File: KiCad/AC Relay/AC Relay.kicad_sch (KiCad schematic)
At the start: 17 parts, among them J1 Screw_Terminal_01x02, J2 Conn_01x06_Female, J3 Screw_Terminal_01x02, K1 1-2071556-1, Q1 FDN537N, SW1 SW_Push, U1 BU33SD5WG-TR, U2 ESP-12E, U3 HLK-PM01

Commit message: initial commit
this is the intitial commit
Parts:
- U2: now not fitted

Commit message: title edited
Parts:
- U2: now fitted
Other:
- title: AC Relay -> BDBM

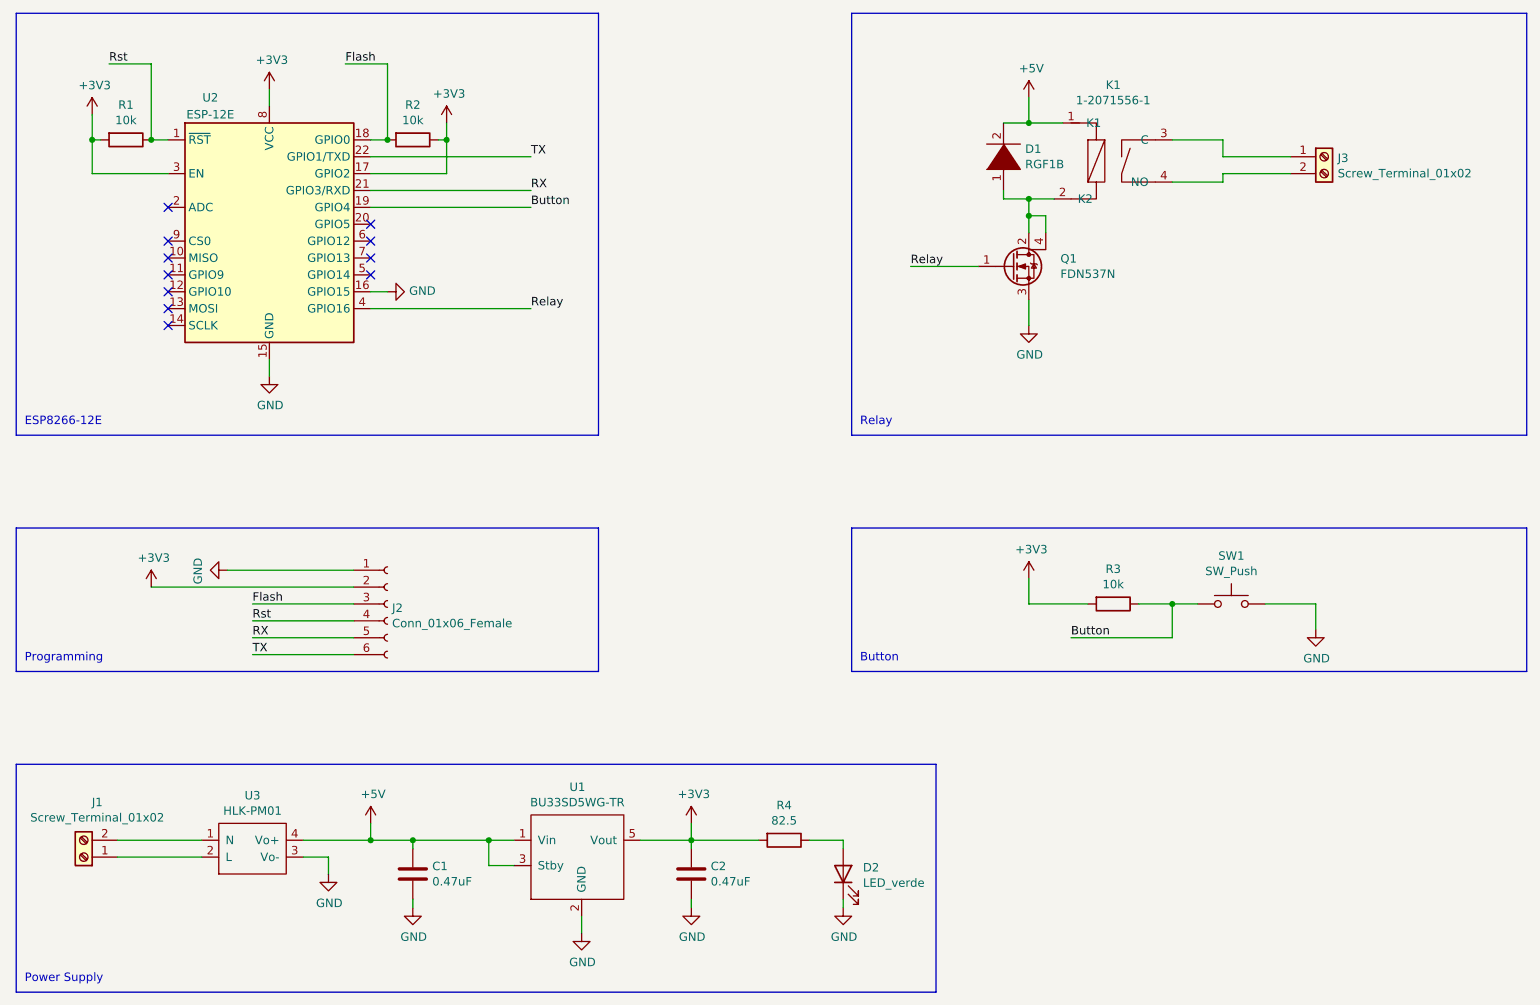
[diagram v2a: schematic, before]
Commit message: until components placemaent
done all until com placement, but had isssue in edge cut .
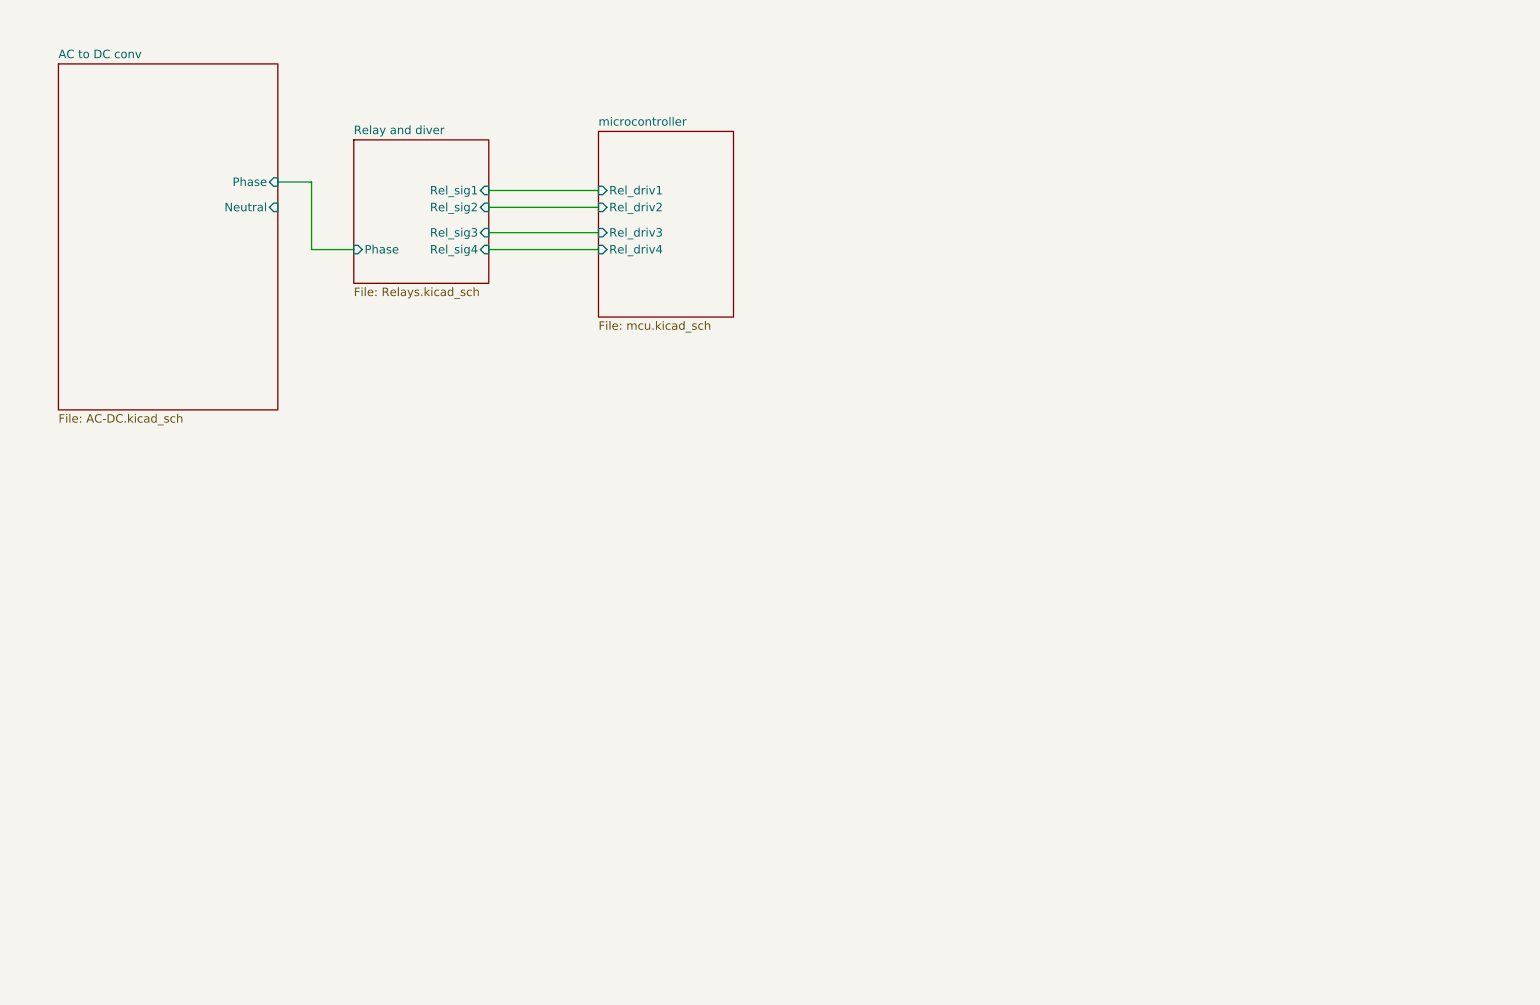
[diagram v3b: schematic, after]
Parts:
- removed C1, C2: 0.47uF, Capacitor_SMD:C_0603_1608Metric, symbol Device:C
- removed D1: RGF1B, Diode_SMD:D_0603_1608Metric, symbol pspice:DIODE
- removed D2: LED_verde, LED_SMD:LED_0603_1608Metric, symbol Device:LED
- removed J1, J3: Screw_Terminal_01x02, TerminalBlock:TerminalBlock_Altech_AK300-2_P5.00mm, symbol Connector:Screw_Terminal_01x02
- removed J2: Conn_01x06_Female, Connector_PinHeader_2.54mm:PinHeader_1x06_P2.54mm_Vertical, symbol Connector:Conn_01x06_Female
- removed K1: 1-2071556-1, red:Rele-1461492-2, symbol AC-Relay-rescue:Relay-red-MQTT-and-Google-Home-from-RED-rescue-AC-Relay-rescue-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
- removed Q1: FDN537N, Package_TO_SOT_SMD:SOT-223, symbol Device:Q_NMOS_GDSD
- removed R1, R2, R3: 10k, Resistor_SMD:R_0603_1608Metric_Pad1.05x0.95mm_HandSolder, symbol Device:R
- removed R4: 82.5, Resistor_SMD:R_0603_1608Metric_Pad1.05x0.95mm_HandSolder, symbol Device:R
- removed SW1: SW_Push, Button_Switch_SMD:SW_SPST_EVQP2, symbol Switch:SW_Push
- removed U1: BU33SD5WG-TR, Package_SO:TSOP-5_1.65x3.05mm_P0.95mm, symbol red:BU33SD5WG-TR
- removed U2: ESP-12E, RF_Module:ESP-12E, symbol RF_Module:ESP-12E
- removed U3: HLK-PM01, red:HLK-PM01, symbol red:HLK-PM01
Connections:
- no-connect marks 11 -> 0
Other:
- added sheet AC to DC conv (AC-DC.kicad_sch)
- added sheet Relay and diver (Relays.kicad_sch)
- added sheet microcontroller (mcu.kicad_sch)
- note removed: "Button"
- note removed: "ESP8266-12E"
- note removed: "Power Supply"
- note removed: "Programming"
- note removed: "Relay"

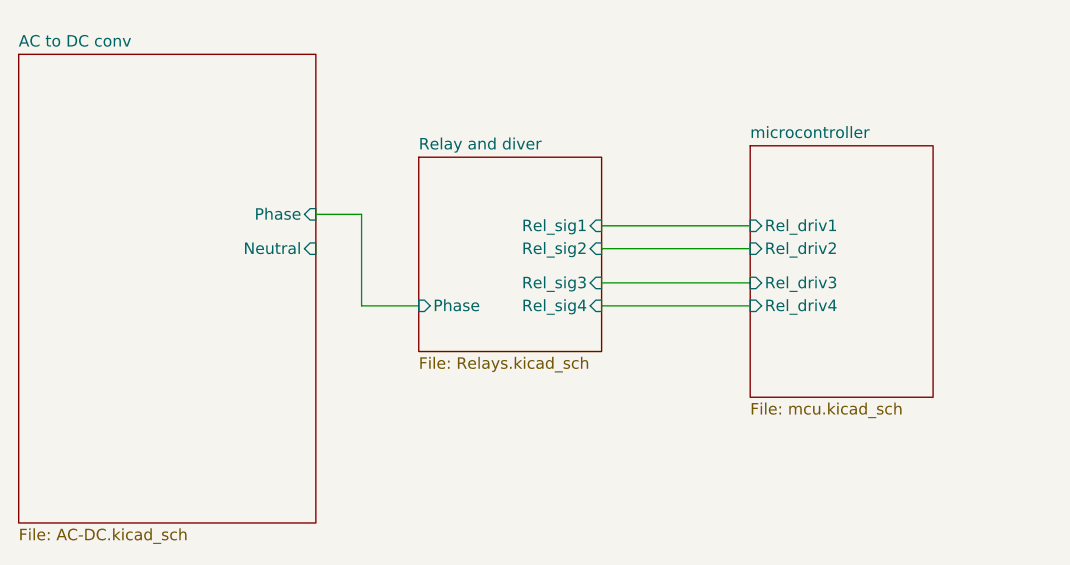
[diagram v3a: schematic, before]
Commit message: error elemination
schametic error elemination
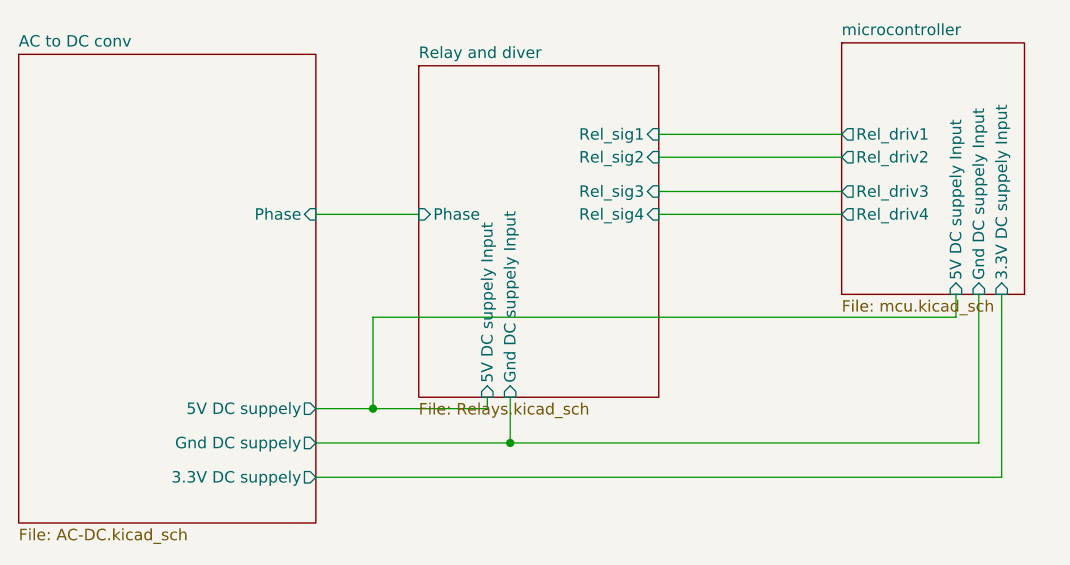
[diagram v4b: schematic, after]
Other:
- sheet AC to DC conv ports: added 3.3V DC suppely, 5V DC suppely, Gnd DC suppely; removed Neutral
- sheet Relay and diver ports: added 5V DC suppely Input, Gnd DC suppely Input; removed none
- sheet microcontroller ports: added 3.3V DC suppely Input, 5V DC suppely Input, Gnd DC suppely Input; removed none
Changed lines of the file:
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@@
 		(comment 1 "Designed by Raksh")
 	)
-	(wire
-		(pts
-			(xy 95.25 59.69) (xy 111.76 59.69)
-		)
-		(stroke
-			(width 0)
-			(type default)
-		)
-	)
-	(wire
-		(pts
-			(xy 68.58 55.88) (xy 63.5 55.88)
-		)
-		(stroke
-			(width 0)
-			(type default)
-		)
-	)
-	(wire
-		(pts
-			(xy 95.25 66.04) (xy 111.76 66.04)
-		)
-		(stroke
-			(width 0)
-			(type default)
-		)
-	)
-	(wire
-		(pts
-			(xy 95.25 57.15) (xy 111.76 57.15)
-		)
-		(stroke
-			(width 0)
-			(type default)
-		)
-	)
-	(wire
-		(pts
-			(xy 74.93 66.04) (xy 68.58 66.04)
-		)
-		(stroke
-			(width 0)
-			(type default)
-		)
-	)
-	(wire
-		(pts
-			(xy 68.58 66.04) (xy 68.58 55.88)
-		)
-		(stroke
-			(width 0)
-			(type default)
-		)
-	)
-	(wire
-		(pts
-			(xy 95.25 63.5) (xy 111.76 63.5)
+	(junction
+		(at 85.09 81.28)
+		(diameter 0)
+		(color 0 0 0 0)
+	)
+	(junction
+		(at 69.85 77.47)
+		(diameter 0)
+		(color 0 0 0 0)
+	)
+	(wire
+		(pts
+			(xy 85.09 81.28) (xy 85.09 76.2)
+		)
+		(stroke
+			(width 0)
+			(type default)
+		)
+	)
+	(wire
+		(pts
+			(xy 69.85 67.31) (xy 134.62 67.31)
+		)
+		(stroke
+			(width 0)
+			(type default)
+		)
+	)
+	(wire
+		(pts
+			(xy 63.5 81.28) (xy 85.09 81.28)
+		)
+		(stroke
+			(width 0)
+			(type default)
+		)
+	)
+	(wire
+		(pts
+			(xy 63.5 77.47) (xy 69.85 77.47)
+		)
+		(stroke
+			(width 0)
+			(type default)
+		)
+	)
+	(wire
+		(pts
+			(xy 63.5 55.88) (xy 74.93 55.88)
+		)
+		(stroke
+			(width 0)
+			(type default)
+		)
+	)
+	(wire
+		(pts
+			(xy 101.6 46.99) (xy 121.92 46.99)
+		)
+		(stroke
+			(width 0)
+			(type default)
+		)
+	)
+	(wire
+		(pts
+			(xy 121.92 53.34) (xy 101.6 53.34)
+		)
+		(stroke
+			(width 0)
+			(type default)
+		)
+	)
+	(wire
+		(pts
+			(xy 69.85 77.47) (xy 69.85 67.31)
+		)
+		(stroke
+			(width 0)
+			(type default)
+		)
+	)
+	(wire
+		(pts
+			(xy 134.62 67.31) (xy 134.62 64.77)
+		)
+		(stroke
+			(width 0)
+			(type default)
+		)
+	)
+	(wire
+		(pts
+			(xy 85.09 81.28) (xy 137.16 81.28)
+		)
+		(stroke
+			(width 0)
+			(type default)
+		)
+	)
+	(wire
+		(pts
+			(xy 139.7 64.77) (xy 139.7 85.09)
+		)
+		(stroke
+			(width 0)
+			(type default)
+		)
+	)
+	(wire
+		(pts
+			(xy 139.7 85.09) (xy 63.5 85.09)
+		)
+		(stroke
+			(width 0)
+			(type default)
+		)
+	)
+	(wire
+		(pts
+			(xy 101.6 49.53) (xy 121.92 49.53)
+		)
+		(stroke
+			(width 0)
+			(type default)
+		)
+	)
+	(wire
+		(pts
+			(xy 121.92 55.88) (xy 101.6 55.88)
+		)
+		(stroke
+			(width 0)
+			(type default)
+		)
+	)
+	(wire
+		(pts
+			(xy 82.55 77.47) (xy 82.55 76.2)
+		)
+		(stroke
+			(width 0)
+			(type default)
+		)
+	)
+	(wire
+		(pts
+			(xy 137.16 81.28) (xy 137.16 64.77)
+		)
+		(stroke
+			(width 0)
+			(type default)
+		)
+	)
+	(wire
+		(pts
+			(xy 69.85 77.47) (xy 82.55 77.47)
 		)
 		(stroke
@@
 			)
 		)
-		(pin "Neutral" input
-			(at 63.5 59.69 0)
+		(pin "3.3V DC suppely" output
+			(at 63.5 85.09 0)
+			(effects
+				(font
+					(size 1.27 1.27)
+				)
+				(justify right)
+			)
+		)
+		(pin "5V DC suppely" output
+			(at 63.5 77.47 0)
+			(effects
+				(font
+					(size 1.27 1.27)
+				)
+				(justify right)
+			)
+		)
+		(pin "Gnd DC suppely" output
+			(at 63.5 81.28 0)
 			(effects
 				(font
@@
 	)
 	(sheet
-		(at 74.93 49.53)
-		(size 20.32 21.59)
+		(at 74.93 39.37)
+		(size 26.67 36.83)
 		(fields_autoplaced yes)
 		(stroke
@@
 		)
 		(property "Sheetname" "Relay and diver"
-			(at 74.93 48.8184 0)
+			(at 74.93 38.6584 0)
 			(effects
 				(font
@@
 		)
 		(property "Sheetfile" "Relays.kicad_sch"
-			(at 74.93 71.7046 0)
+			(at 74.93 76.7846 0)
 			(effects
 				(font
@@
 		)
 		(pin "Rel_sig2" input
-			(at 95.25 59.69 0)
+			(at 101.6 49.53 0)
 			(effects
 				(font
@@
 		)
 		(pin "Phase" input
-			(at 74.93 66.04 180)
+			(at 74.93 55.88 180)
 			(effects
 				(font
@@
 		)
 		(pin "Rel_sig3" input
-			(at 95.25 63.5 0)
+			(at 101.6 53.34 0)
 			(effects
 				(font
@@
 		)
 		(pin "Rel_sig1" input
-			(at 95.25 57.15 0)
+			(at 101.6 46.99 0)
 			(effects
 				(font
@@
 		)
 		(pin "Rel_sig4" input
-			(at 95.25 66.04 0)
-			(effects
-				(font
-					(size 1.27 1.27)
-				)
-				(justify right)
+			(at 101.6 55.88 0)
+			(effects
+				(font
+					(size 1.27 1.27)
+				)
+				(justify right)
+			)
+		)
+		(pin "5V DC suppely Input" input
+			(at 82.55 76.2 270)
+			(effects
+				(font
+					(size 1.27 1.27)
+				)
+				(justify left)
+			)
+		)
+		(pin "Gnd DC suppely Input" input
+			(at 85.09 76.2 270)
+			(effects
+				(font
+					(size 1.27 1.27)
+				)
+				(justify left)
 			)
 		)
@@
 	)
 	(sheet
-		(at 111.76 48.26)
+		(at 121.92 36.83)
 		(size 20.32 27.94)
 		(fields_autoplaced yes)
@@
 		)
 		(property "Sheetname" "microcontroller"
-			(at 111.76 47.5484 0)
+			(at 121.92 36.1184 0)
 			(effects
 				(font
@@
 		)
 		(property "Sheetfile" "mcu.kicad_sch"
-			(at 111.76 76.7846 0)
+			(at 121.92 65.3546 0)
 			(effects
 				(font
@@
 			)
 		)
-		(pin "Rel_driv2" input
-			(at 111.76 59.69 180)
-			(effects
-				(font
-					(size 1.27 1.27)
-				)
-				(justify left)
-			)
-		)
-		(pin "Rel_driv3" input
-			(at 111.76 63.5 180)
-			(effects
-				(font
-					(size 1.27 1.27)
-				)
-				(justify left)
-			)
-		)
-		(pin "Rel_driv1" input
-			(at 111.76 57.15 180)
-			(effects
-				(font
-					(size 1.27 1.27)
-				)
-				(justify left)
-			)
-		)
-		(pin "Rel_driv4" input
-			(at 111.76 66.04 180)
-			(effects
-				(font
+		(pin "5V DC suppely Input" input
+			(at 134.62 64.77 270)
+			(effects
+				(font
+					(size 1.27 1.27)
+				)
+				(justify left)
+			)
+		)
+		(pin "Gnd DC suppely Input" input
+			(at 137.16 64.77 270)
+			(effects
+				(font
+					(size 1.27 1.27)
+				)
+				(justify left)
+			)
+		)
+		(pin "3.3V DC suppely Input" input
+			(at 139.7 64.77 270)
+			(effects
+				(font
+					(size 1.27 1.27)
+				)
+				(justify left)
+			)
+		)
+		(pin "Rel_driv3" output
+			(at 121.92 53.34 180)
+			(effects
+				(font
+					(size 1.27 1.27)
+				)
+				(justify left)
+			)
+		)
+		(pin "Rel_driv1" output
+			(at 121.92 46.99 180)
+			(effects
+				(font
+					(size 1.27 1.27)
+				)
+				(justify left)
+			)
+		)
+		(pin "Rel_driv4" output
+			(at 121.92 55.88 180)
+			(effects
+				(font
+					(size 1.27 1.27)
+				)
+				(justify left)
+			)
+		)
+		(pin "Rel_driv2" output
+			(at 121.92 49.53 180)
+			(effects
+				(font
